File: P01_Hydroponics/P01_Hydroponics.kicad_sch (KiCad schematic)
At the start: 2 parts, among them U1 IR4301, U2 IR4301

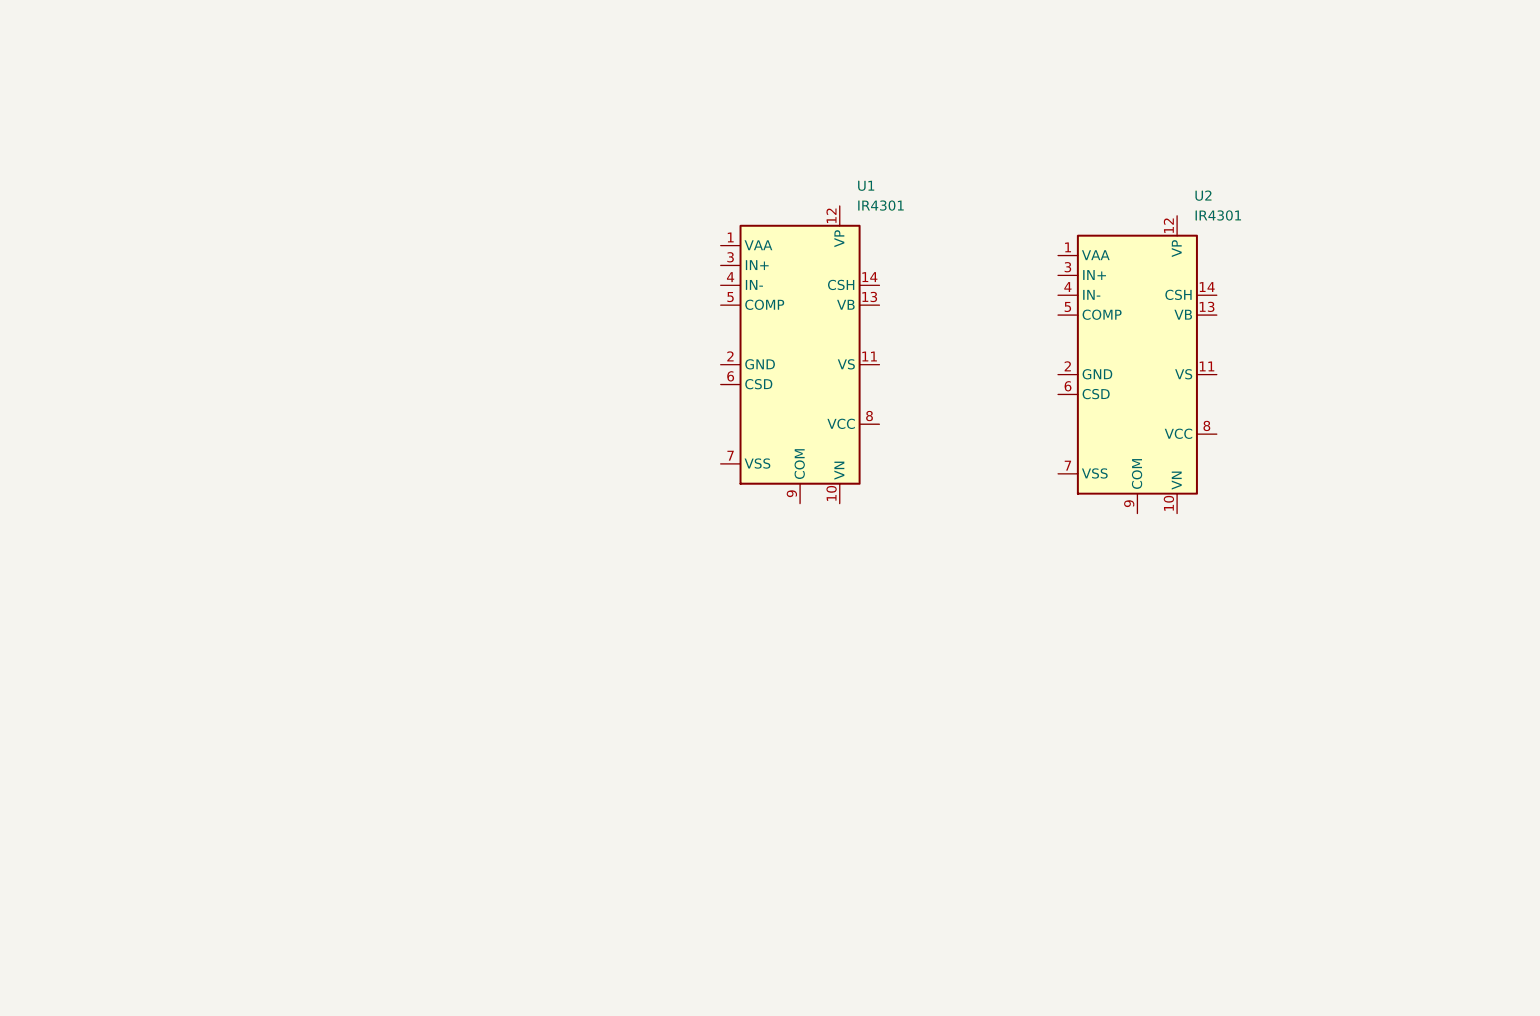
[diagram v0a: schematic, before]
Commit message: Second commit
need some idea's for the power path
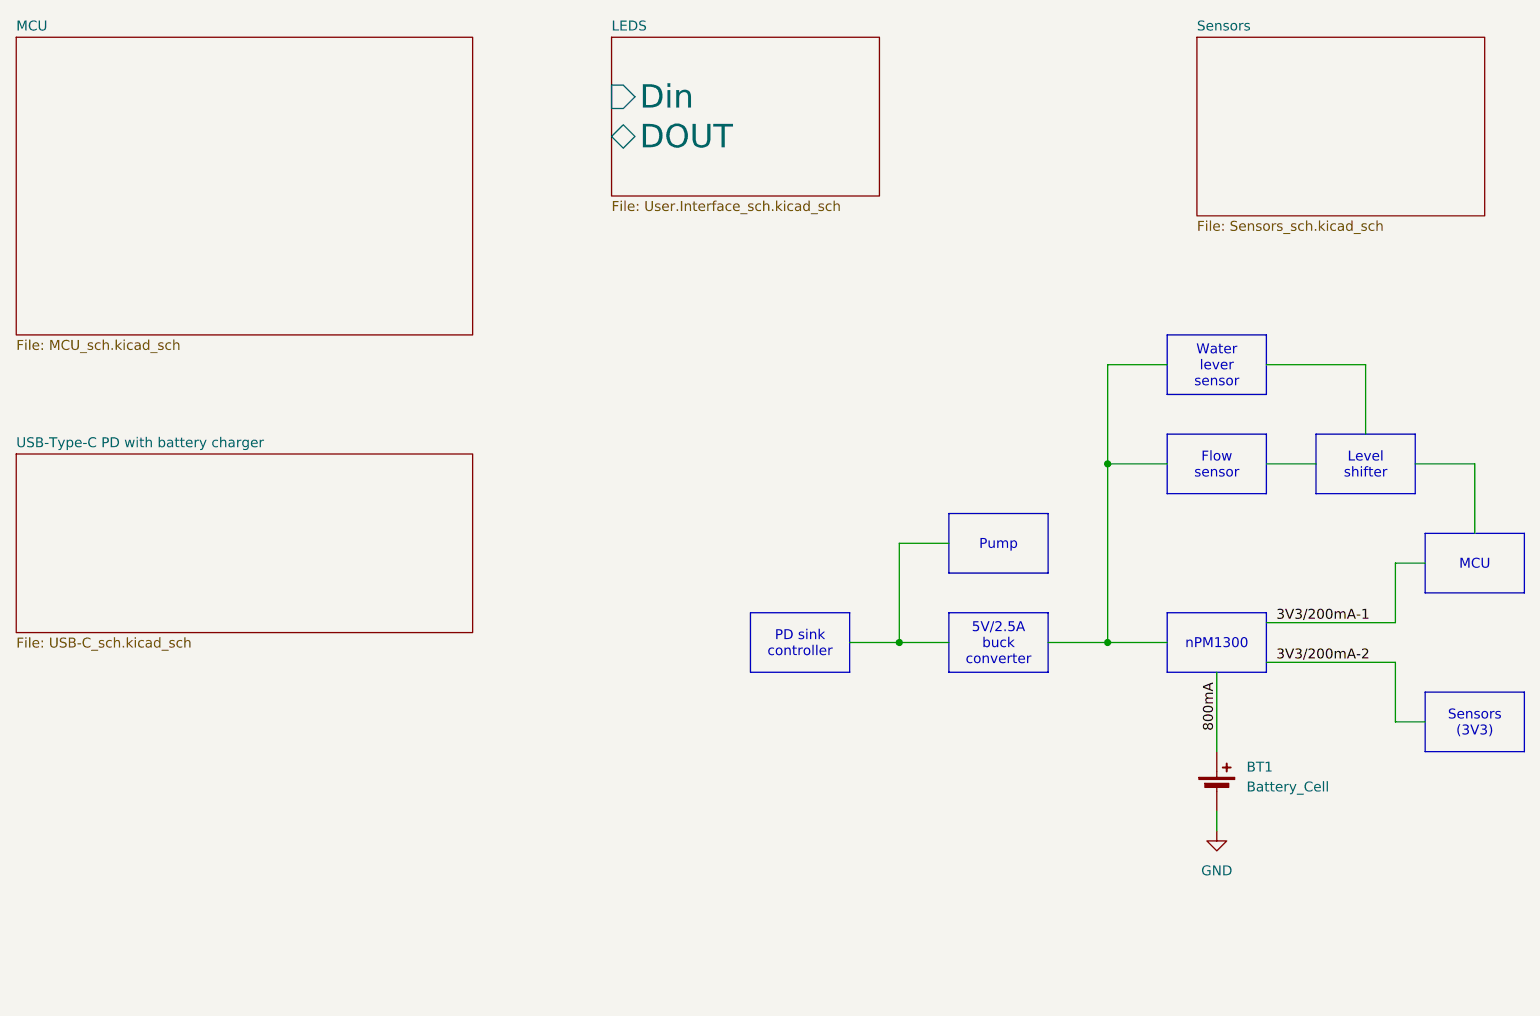
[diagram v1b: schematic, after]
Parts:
- removed U1, U2: IR4301, Package_DFN_QFN:Infineon_PQFN-22-15-4EP_6x5mm_P0.65mm, symbol Amplifier_Audio:IR4301
- added BT1: Battery_Cell, symbol Device:Battery_Cell
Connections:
- new net 800mA: BT1.1 (+)
- new net GND: BT1.2 (-)
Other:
- added sheet LEDS (User.Interface_sch.kicad_sch)
- added sheet MCU (MCU_sch.kicad_sch)
- added sheet Sensors (Sensors_sch.kicad_sch)
- added sheet USB-Type-C PD with battery charger (USB-C_sch.kicad_sch)
- company: (none) -> NekoCo
- title: (none) -> Main

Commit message: Update power supply scheme
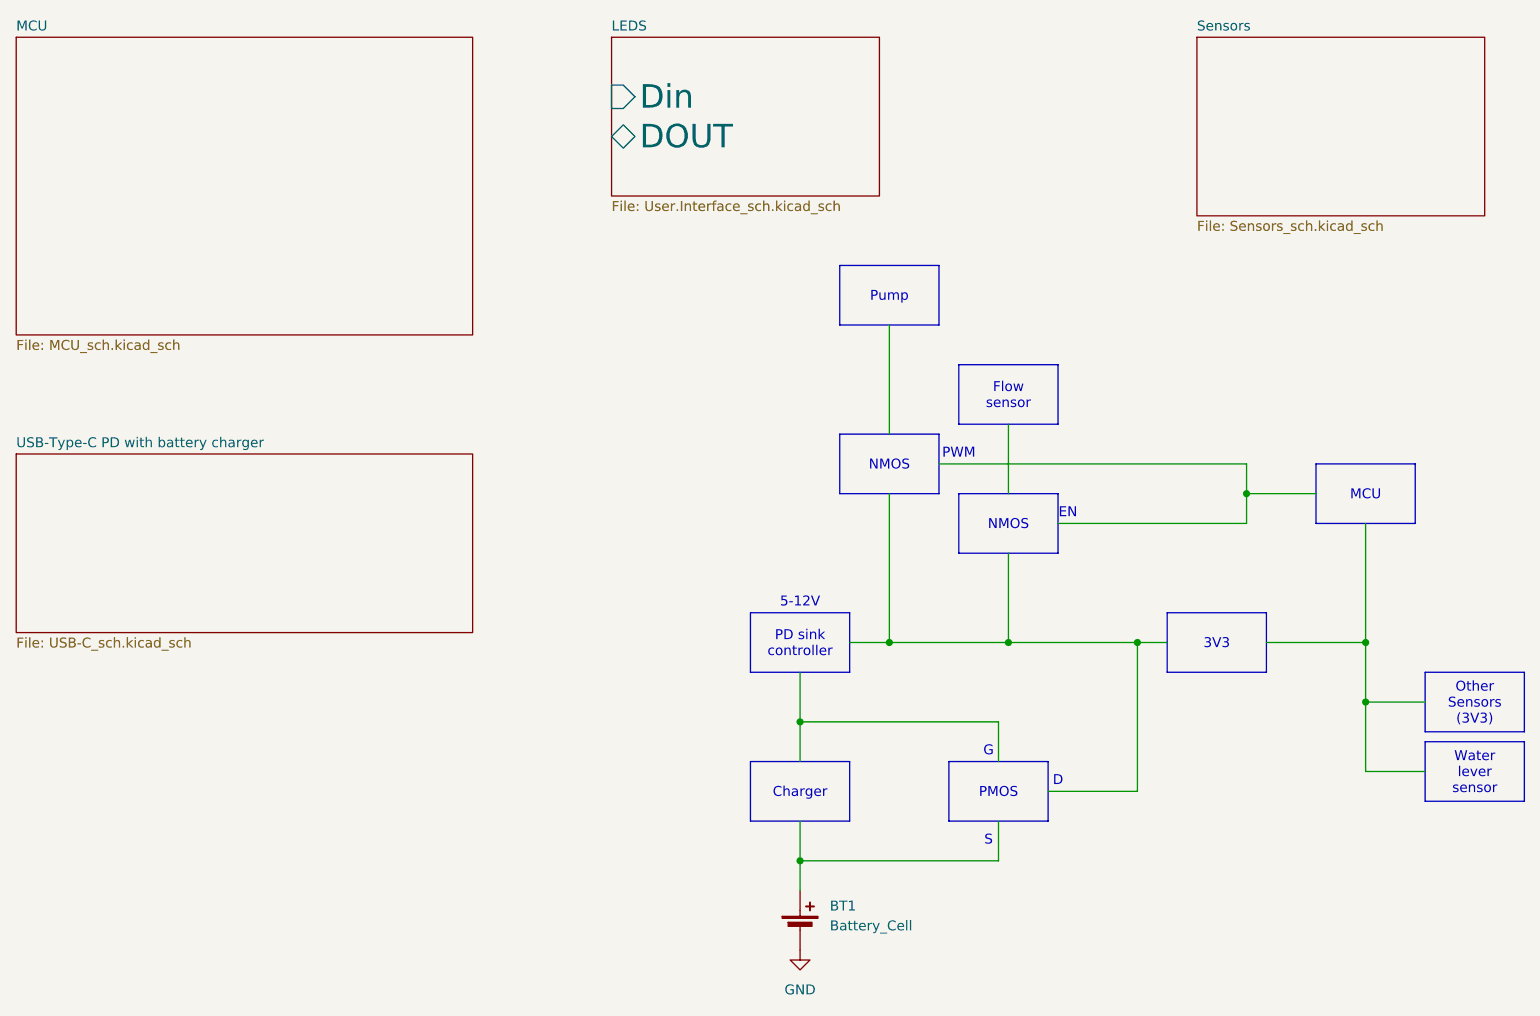
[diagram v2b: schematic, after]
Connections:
- net 800mA: no longer names the net of BT1.1 (+)
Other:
- note added: "5-12V"
- note added: "D"
- note added: "EN"
- note added: "G"
- note added: "PWM"
- note added: "S"
